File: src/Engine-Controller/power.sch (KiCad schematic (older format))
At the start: 21 parts, among them P1 EJ508A, U2 LM22672MRE-5.0_NOPB, U3 LMS8117AMP-3.3_NOPB

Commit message: Added Flash
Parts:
- added None?: 5V, symbol Engine-Controller:5V
- added None?: 3.3V, symbol Engine-Controller:3.3V
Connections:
- wire segments 54 -> 56
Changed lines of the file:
@@
 $Descr A4 11693 8268
 encoding utf-8
-Sheet 2 5
+Sheet 2 6
 Title "Engine Microcontroller Power Supply"
 Date ""
@@
 Wire Wire Line
 	8100 4550 8100 4300
+$Comp
+L Engine-Controller:5V None?
+U 1 1 61790759
+P 7550 3700
+F 0 "None?" H 7678 3689 50  0001 L CNN
+F 1 "5V" H 7500 3800 50  0000 L CNN
+F 2 "" H 7550 3700 50  0001 C CNN
+F 3 "" H 7550 3700 50  0001 C CNN
+	1    7550 3700
+	1    0    0    -1
+$EndComp
+Wire Wire Line
+	7550 4000 7550 3850
+$Comp
+L Engine-Controller:3.3V None?
+U 1 1 6179CDBA
+P 8700 3750
+F 0 "None?" H 8828 3739 50  0001 L CNN
+F 1 "3.3V" H 8622 3853 50  0000 L CNN
+F 2 "" H 8700 3750 50  0001 C CNN
+F 3 "" H 8700 3750 50  0001 C CNN
+	1    8700 3750
+	1    0    0    -1
+$EndComp
+Wire Wire Line
+	8700 4000 8700 3900
 $EndSCHEMATC

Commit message: Added Micro SD Card
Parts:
- gave numbers to parts that had none: 2
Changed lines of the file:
@@
 	8100 4550 8100 4300
 $Comp
-L Engine-Controller:5V None?
+L Engine-Controller:5V None03
 U 1 1 61790759
 P 7550 3700
-F 0 "None?" H 7678 3689 50  0001 L CNN
+F 0 "None03" H 7678 3689 50  0001 L CNN
 F 1 "5V" H 7500 3800 50  0000 L CNN
 F 2 "" H 7550 3700 50  0001 C CNN
@@
 	7550 4000 7550 3850
 $Comp
-L Engine-Controller:3.3V None?
+L Engine-Controller:3.3V None04
 U 1 1 6179CDBA
 P 8700 3750
-F 0 "None?" H 8828 3739 50  0001 L CNN
+F 0 "None04" H 8828 3739 50  0001 L CNN
 F 1 "3.3V" H 8622 3853 50  0000 L CNN
 F 2 "" H 8700 3750 50  0001 C CNN

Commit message: Fixed Schematic ERC erros
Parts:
- removed None03: 5V, symbol Engine-Controller:5V
- removed None04: 3.3V, symbol Engine-Controller:3.3V
- U3: footprint Engine-Controller:SOT-223 -> (none)
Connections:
- wire segments 56 -> 54
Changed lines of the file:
@@
-$EndComp
-$Comp
-L Engine-Controller:LMS8117AMP-3.3_NOPB U3
-U 1 1 60EBB9CF
-P 8100 4050
-F 0 "U3" H 8100 4250 50  0000 C CNN
-F 1 "LMS8117AMP-3.3_NOPB" H 8100 4274 50  0001 C CNN
-F 2 "Engine-Controller:SOT-223" H 8100 4050 50  0001 C CNN
-F 3 "" H 8100 4050 50  0001 C CNN
-	1    8100 4050
-	1    0    0    -1
 $EndComp
 $Comp
@@
 	7750 4000 7550 4000
 Connection ~ 7550 4000
+Connection ~ 8700 4000
+Wire Wire Line
+	8100 4550 8100 4300
+$Comp
+L Engine-Controller:LMS8117AMP-3.3_NOPB U3
+U 1 1 61E22A22
+P 8100 4050
+F 0 "U3" H 8100 4365 50  0000 C CNN
+F 1 "LMS8117AMP-3.3_NOPB" H 8100 4274 50  0000 C CNN
+F 2 "" H 8100 4050 50  0001 C CNN
+F 3 "" H 8100 4050 50  0001 C CNN
+	1    8100 4050
+	1    0    0    -1
+$EndComp
 Wire Wire Line
 	8450 4000 8700 4000
-Connection ~ 8700 4000
-Wire Wire Line
-	8100 4550 8100 4300
-$Comp
-L Engine-Controller:5V None03
-U 1 1 61790759
-P 7550 3700
-F 0 "None03" H 7678 3689 50  0001 L CNN
-F 1 "5V" H 7500 3800 50  0000 L CNN
-F 2 "" H 7550 3700 50  0001 C CNN
-F 3 "" H 7550 3700 50  0001 C CNN
-	1    7550 3700
-	1    0    0    -1
-$EndComp
-Wire Wire Line
-	7550 4000 7550 3850
-$Comp
-L Engine-Controller:3.3V None04
-U 1 1 6179CDBA
-P 8700 3750
-F 0 "None04" H 8828 3739 50  0001 L CNN
-F 1 "3.3V" H 8622 3853 50  0000 L CNN
-F 2 "" H 8700 3750 50  0001 C CNN
-F 3 "" H 8700 3750 50  0001 C CNN
-	1    8700 3750
-	1    0    0    -1
-$EndComp
-Wire Wire Line
-	8700 4000 8700 3900
 $EndSCHEMATC

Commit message: Routed decoupling caps
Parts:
- P1: footprint (none) -> Engine-Controller:12V_power_jack
- U3: footprint (none) -> Engine-Controller:SOT-223
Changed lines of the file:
@@
 F 0 "P1" H 2207 3917 50  0000 C CNN
 F 1 "EJ508A" H 2207 3826 50  0000 C CNN
-F 2 "" H 2200 3560 50  0001 C CNN
+F 2 "Engine-Controller:12V_power_jack" H 2200 3560 50  0001 C CNN
 F 3 "~" H 2200 3560 50  0001 C CNN
 	1    2150 3600
@@
 F 0 "U3" H 8100 4365 50  0000 C CNN
 F 1 "LMS8117AMP-3.3_NOPB" H 8100 4274 50  0000 C CNN
-F 2 "" H 8100 4050 50  0001 C CNN
+F 2 "Engine-Controller:SOT-223" H 8100 4050 50  0001 C CNN
 F 3 "" H 8100 4050 50  0001 C CNN
 	1    8100 4050

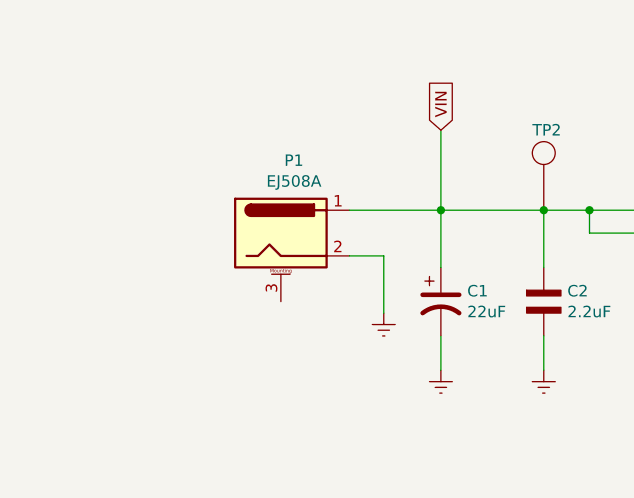
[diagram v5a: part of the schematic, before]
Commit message: Added voltage source selector to schematic
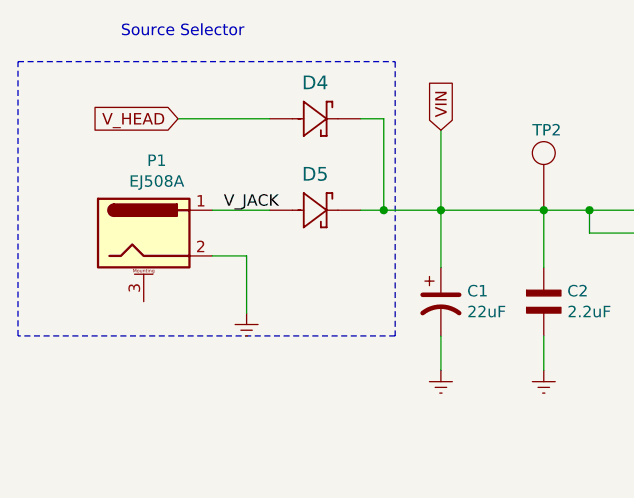
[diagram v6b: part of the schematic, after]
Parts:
- added D4, D5: SM5819PL-TP, SOD-123FL_MCC, symbol Engine-Controller:SM5819PL-TP
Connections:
- net VIN: now also D4.1, D5.1; no longer P1.1
- new net V_HEAD: D4.2
- new net V_JACK: D5.2, P1.1
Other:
- note added: "Source Selector\n"
- moved on the sheet: P1
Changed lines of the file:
@@
 L power:Earth #PWR0103
 U 1 1 60EC7BCD
-P 2600 3950
-F 0 "#PWR0103" H 2600 3700 50  0001 C CNN
-F 1 "Earth" H 2600 3800 50  0001 C CNN
-F 2 "" H 2600 3950 50  0001 C CNN
-F 3 "~" H 2600 3950 50  0001 C CNN
-	1    2600 3950
-	1    0    0    -1
-$EndComp
-Wire Wire Line
-	2450 3700 2600 3700
+P 2000 3950
+F 0 "#PWR0103" H 2000 3700 50  0001 C CNN
+F 1 "Earth" H 2000 3800 50  0001 C CNN
+F 2 "" H 2000 3950 50  0001 C CNN
+F 3 "~" H 2000 3950 50  0001 C CNN
+	1    2000 3950
+	1    0    0    -1
+$EndComp
+Wire Wire Line
+	1850 3700 2000 3700
 Text GLabel 2850 3150 1    50   Input ~ 0
 VIN
@@
 	2850 3150 2850 3500
 Connection ~ 2850 3500
-Wire Wire Line
-	2850 3500 2450 3500
 $Comp
 L Engine-Controller:UKL1C220KDDANATD C1
@@
 L Engine-Controller:EJ508A P1
 U 1 1 60E212B8
-P 2150 3600
-F 0 "P1" H 2207 3917 50  0000 C CNN
-F 1 "EJ508A" H 2207 3826 50  0000 C CNN
-F 2 "Engine-Controller:12V_power_jack" H 2200 3560 50  0001 C CNN
-F 3 "~" H 2200 3560 50  0001 C CNN
-	1    2150 3600
-	1    0    0    -1
-$EndComp
-Wire Wire Line
-	2600 3700 2600 3950
+P 1550 3600
+F 0 "P1" H 1607 3917 50  0000 C CNN
+F 1 "EJ508A" H 1607 3826 50  0000 C CNN
+F 2 "Engine-Controller:12V_power_jack" H 1600 3560 50  0001 C CNN
+F 3 "~" H 1600 3560 50  0001 C CNN
+	1    1550 3600
+	1    0    0    -1
+$EndComp
+Wire Wire Line
+	2000 3700 2000 3950
 Wire Wire Line
 	6650 4000 7050 4000
@@
 Wire Wire Line
 	8450 4000 8700 4000
+$Comp
+L Engine-Controller:SM5819PL-TP D5
+U 1 1 60EEFB5B
+P 2100 3500
+F 0 "D5" H 2300 3657 60  0000 C CNN
+F 1 "SM5819PL-TP" H 2350 3300 60  0001 C CNN
+F 2 "SOD-123FL_MCC" H 2350 3200 60  0001 C CNN
+F 3 "" H 2100 3500 60  0001 C CNN
+	1    2100 3500
+	1    0    0    -1
+$EndComp
+Wire Wire Line
+	1850 3500 2100 3500
+Wire Wire Line
+	2500 3500 2600 3500
+Text Label 1900 3500 0    50   ~ 0
+V_JACK
+Text GLabel 1700 3100 0    50   Input ~ 0
+V_HEAD
+$Comp
+L Engine-Controller:SM5819PL-TP D4
+U 1 1 60EF8AF2
+P 2100 3100
+F 0 "D4" H 2300 3257 60  0000 C CNN
+F 1 "SM5819PL-TP" H 2350 2900 60  0001 C CNN
+F 2 "SOD-123FL_MCC" H 2350 2800 60  0001 C CNN
+F 3 "" H 2100 3100 60  0001 C CNN
+	1    2100 3100
+	1    0    0    -1
+$EndComp
+Wire Wire Line
+	1700 3100 2100 3100
+Wire Wire Line
+	2500 3100 2600 3100
+Wire Wire Line
+	2600 3100 2600 3500
+Connection ~ 2600 3500
+Wire Wire Line
+	2600 3500 2850 3500
+Wire Notes Line
+	2650 2850 2650 4050
+Wire Notes Line
+	2650 4050 1000 4050
+Wire Notes Line
+	1000 4050 1000 2850
+Wire Notes Line
+	1000 2850 2650 2850
+Text Notes 1450 2750 0    50   ~ 0
+Source Selector\n
 $EndSCHEMATC

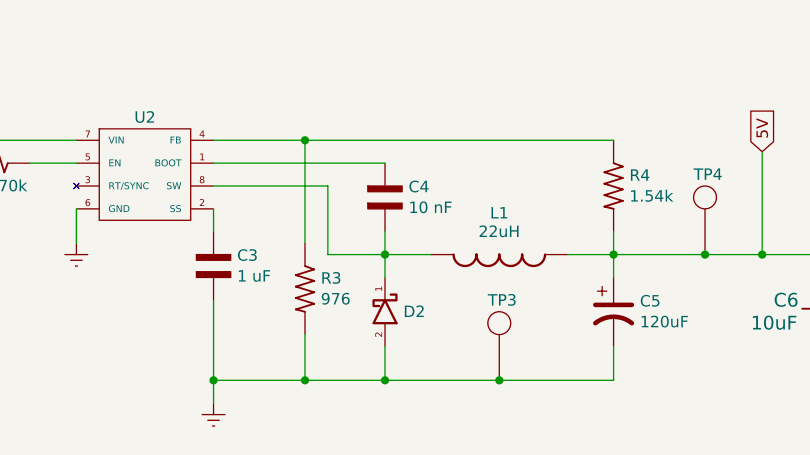
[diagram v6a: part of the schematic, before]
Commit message: Updated buck converter schottky symbol
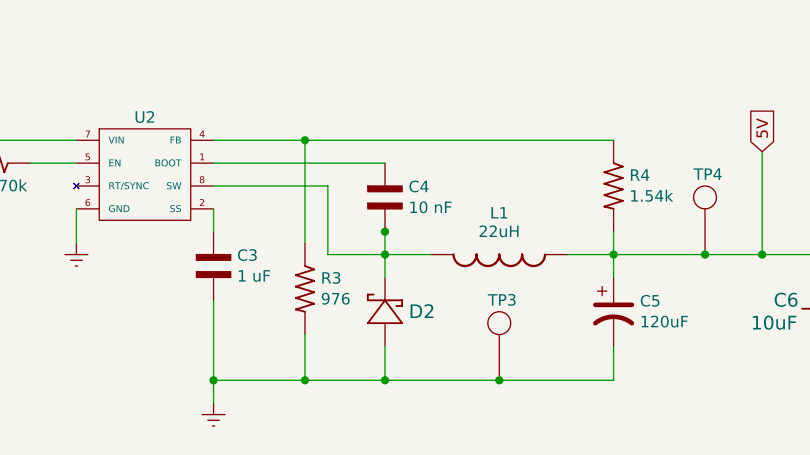
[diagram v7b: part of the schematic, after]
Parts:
- removed D2: Schottky, Engine-Controller:RB160VAM-60TR, symbol Engine-Controller:Schottky
- added D2: RB160VAM-60TR, SOD-123FL_MCC, symbol Engine-Controller:RB160VAM-60TR
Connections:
- net Earth: now also D2.2
- net at C4.1, L1.1, U2.8 (SW): now also D2.1
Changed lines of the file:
@@
-$EndComp
-$Comp
-L Engine-Controller:Schottky D2
-U 1 1 611BBBEC
-P 5650 4250
-F 0 "D2" V 5650 4330 50  0000 L CNN
-F 1 "Schottky" V 5695 4330 50  0001 L CNN
-F 2 "Engine-Controller:RB160VAM-60TR" H 5650 4250 50  0001 C CNN
-F 3 "" H 5650 4250 50  0001 C CNN
-	1    5650 4250
-	0    1    1    0
 $EndComp
 $Comp
@@
 Text Notes 1450 2750 0    50   ~ 0
 Source Selector\n
+$Comp
+L Engine-Controller:RB160VAM-60TR D2
+U 1 1 60F4329D
+P 5650 4450
+F 0 "D2" V 5850 4346 60  0000 R CNN
+F 1 "RB160VAM-60TR" H 5900 4250 60  0001 C CNN
+F 2 "SOD-123FL_MCC" H 5900 4150 60  0001 C CNN
+F 3 "" H 5650 4450 60  0001 C CNN
+	1    5650 4450
+	0    -1   -1   0
+$EndComp
+Connection ~ 5650 3900
 $EndSCHEMATC

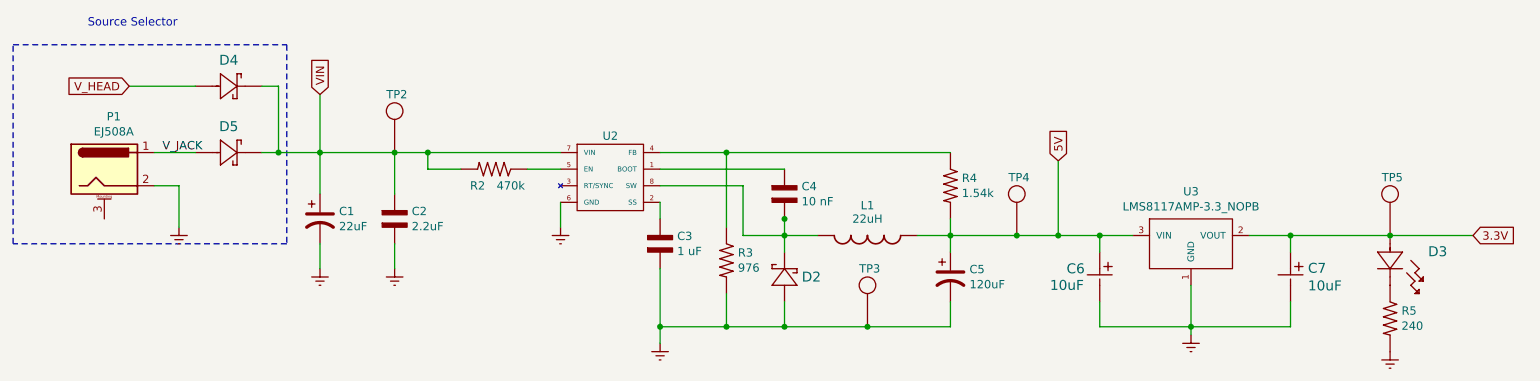
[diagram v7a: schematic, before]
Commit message: Grounded 12V barrel plug detect pin to GND
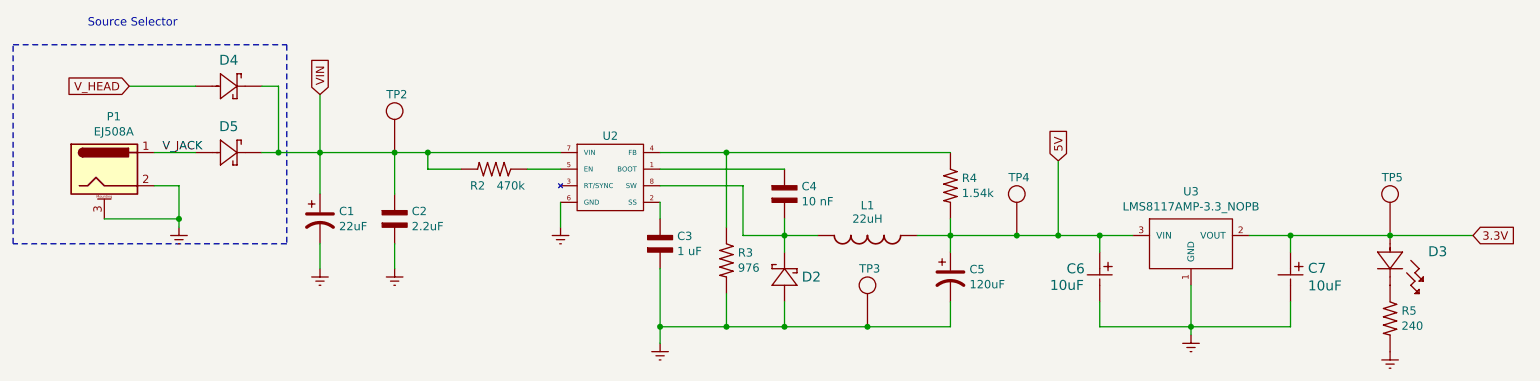
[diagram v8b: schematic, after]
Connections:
- net Earth: now also P1.3 (MountPin)
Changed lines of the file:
@@
 $EndComp
 Wire Wire Line
-	2000 3700 2000 3950
+	2000 3700 2000 3900
 Wire Wire Line
 	6650 4000 7050 4000
@@
 	0    -1   -1   0
 $EndComp
-Connection ~ 5650 3900
+Wire Wire Line
+	1550 3900 2000 3900
+Connection ~ 2000 3900
+Wire Wire Line
+	2000 3900 2000 3950
 $EndSCHEMATC
